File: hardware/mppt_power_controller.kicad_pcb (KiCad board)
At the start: 2 copper layers, 100 x 50 mm, 61 parts, among them J2 USB_B_Micro, J3 Conn_ARM_JTAG_SWD_10, J5 Curiosity Board, Q1 Q_NMOS_GSD, Q2 Q_NMOS_GSD, U1 INA233, U2 PX3519, U3 ATSAMD21G18A-AUT, U4 INA233, U5 TPS61090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

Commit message: Flip solar panel connector around so pin 1 is power and pin 2 is ground like every other board with JST connectors.
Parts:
- J1: renamed from Solar In
- J4: renamed from Battery Out
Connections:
- J1 pad 1: GND -> Net-(C2-Pad2)
- J1 pad 2: Net-(C2-Pad2) -> GND
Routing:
- net Net-(C2-Pad2): track 14.5 -> 15.4 mm
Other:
- rule pad_to_mask_clearance: 0.051 -> 0
- board text added: "Battery"
- board text added: "Solar"
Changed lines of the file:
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@@
   (general
     (thickness 1.6)
-    (drawings 61)
-    (tracks 465)
+    (drawings 63)
+    (tracks 467)
     (modules 61)
     (nets 69)
@@
       (dielectric_constraints no)
     )
-    (last_trace_width 0.3)
+    (last_trace_width 0.75)
     (user_trace_width 0.2)
     (user_trace_width 0.25)
@@
     (pad_size 1.524 1.524)
     (pad_drill 0.762)
-    (pad_to_mask_clearance 0.051)
-    (solder_mask_min_width 0.25)
+    (pad_to_mask_clearance 0)
     (aux_axis_origin 0 0)
     (visible_elements 7FFDFFFF)
@@
     (descr "JST PH series connector, S2B-PH-K (http://www.jst-mfg.com/product/pdf/eng/ePH.pdf), generated with kicad-footprint-generator")
     (tags "connector JST PH top entry")
-    (fp_text reference "Battery Out" (at -2.7 2.35 180) (layer "F.SilkS")
+    (fp_text reference "J4" (at -2.7 2.35 180) (layer "F.SilkS") hide
       (effects (font (size 0.75 0.75) (thickness 0.15)))
     )
@@
     (descr "JST PH series connector, S2B-PH-K (http://www.jst-mfg.com/product/pdf/eng/ePH.pdf), generated with kicad-footprint-generator")
     (tags "connector JST PH top entry")
-    (fp_text reference "Solar In" (at 4.95 2.35 180) (layer "F.SilkS")
+    (fp_text reference "J1" (at 4.95 2.35 180) (layer "F.SilkS") hide
       (effects (font (size 1 1) (thickness 0.15)))
     )
@@
     )
     (pad "2" thru_hole oval (at 2 0 270) (size 1.2 1.75) (drill 0.75) (layers *.Cu *.Mask)
-      (net 3 "Net-(C2-Pad2)"))
-    (pad "1" thru_hole roundrect (at 0 0 270) (size 1.2 1.75) (drill 0.75) (layers *.Cu *.Mask) (roundrect_rratio 0.208333)
       (net 1 "GND"))
+    (pad "1" thru_hole roundrect (at 0 0 270) (size 1.2 1.75) (drill 0.75) (layers *.Cu *.Mask) (roundrect_rratio 0.208333)
+      (net 3 "Net-(C2-Pad2)"))
     (model "${KISYS3DMOD}/Connector_JST.3dshapes/JST_PH_S2B-PH-K_1x02_P2.00mm_Horizontal.wrl"
       (at (xyz 0 0 0))
@@
     )
   )
+  (gr_text "Battery" (at 166.8 77.25) (layer "F.SilkS")
+    (effects (font (size 1 1) (thickness 0.15)))
+  )
+  (gr_text "Solar" (at 74.55 77.4) (layer "F.SilkS")
+    (effects (font (size 1 1) (thickness 0.15)))
+  )
   (gr_text "FET\nPWM" (at 104.65 84.95) (layer "F.SilkS")
     (effects (font (size 1.5 1.5) (thickness 0.15)))
@@
   (gr_line (start 70 110) (end 170 110) (layer "Edge.Cuts") (width 0.05))
   (gr_line (start 70 60) (end 70 110) (layer "Edge.Cuts") (width 0.05))
+  (segment (start 77.6 72) (end 79.4875 73.8875) (width 0.75) (layer "F.Cu") (net 3))
+  (segment (start 79.4875 73.8875) (end 81.6125 73.8875) (width 0.75) (layer "F.Cu") (net 3))
+  (segment (start 76.45 72) (end 77.6 72) (width 0.75) (layer "F.Cu") (net 3))
   (segment (start 155.771766 78) (end 156.5 77.271766) (width 0.3) (layer "F.Cu") (net 1))
   (segment (start 155.025002 77.274998) (end 155.825002 77.274998) (width 0.25) (layer "F.Cu") (net 34))
@@
   (segment (start 85.9625 75.9125) (end 87.8875 75.9125) (width 0.3) (layer "F.Cu") (net 2))
   (segment (start 81.5 74) (end 81.6125 73.8875) (width 0.75) (layer "F.Cu") (net 3))
-  (segment (start 76.45 74) (end 81.5 74) (width 0.75) (layer "F.Cu") (net 3))
   (segment (start 97.85 77.5) (end 97.85 76.325001) (width 0.5) (layer "F.Cu") (net 4))
   (segment (start 98.375 78.5) (end 98.375 78.025) (width 0.5) (layer "F.Cu") (net 4))

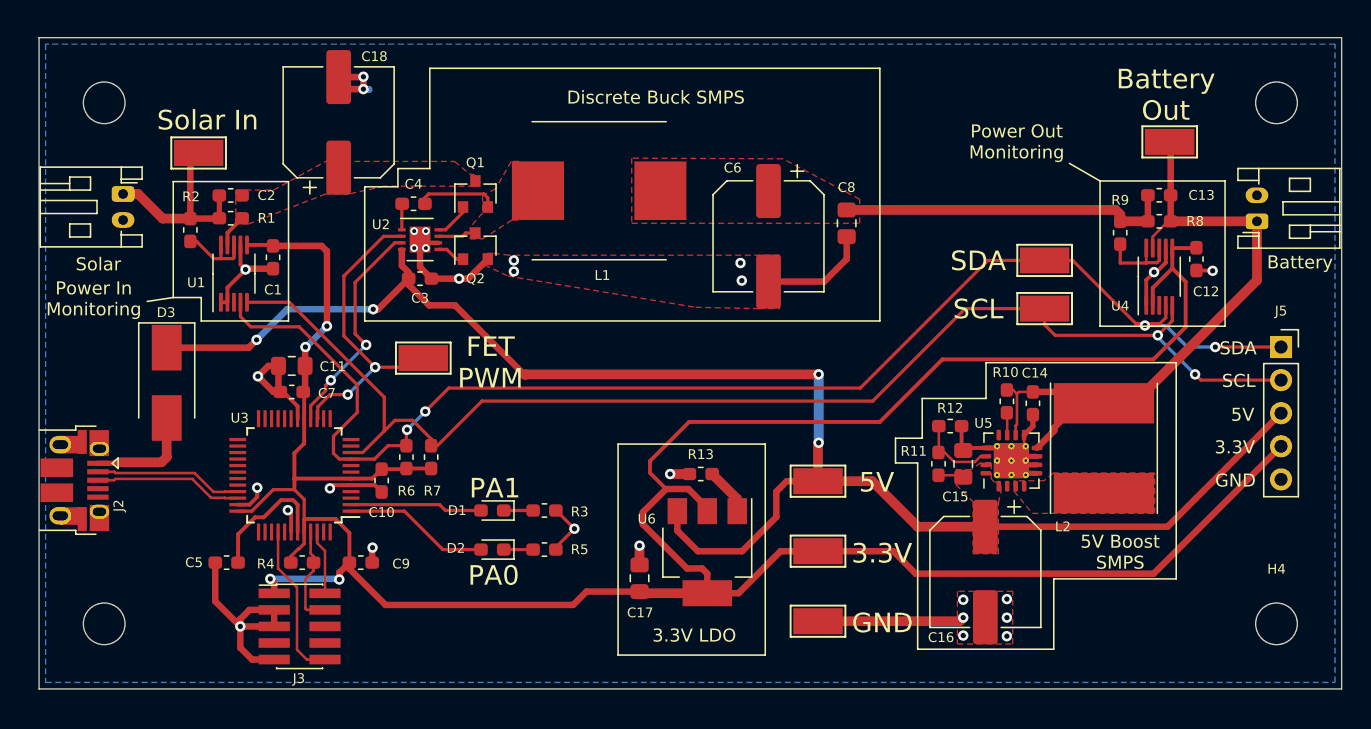
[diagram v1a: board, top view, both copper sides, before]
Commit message: Add some new datasheets, modify code to only flash LEDs as a starting point.
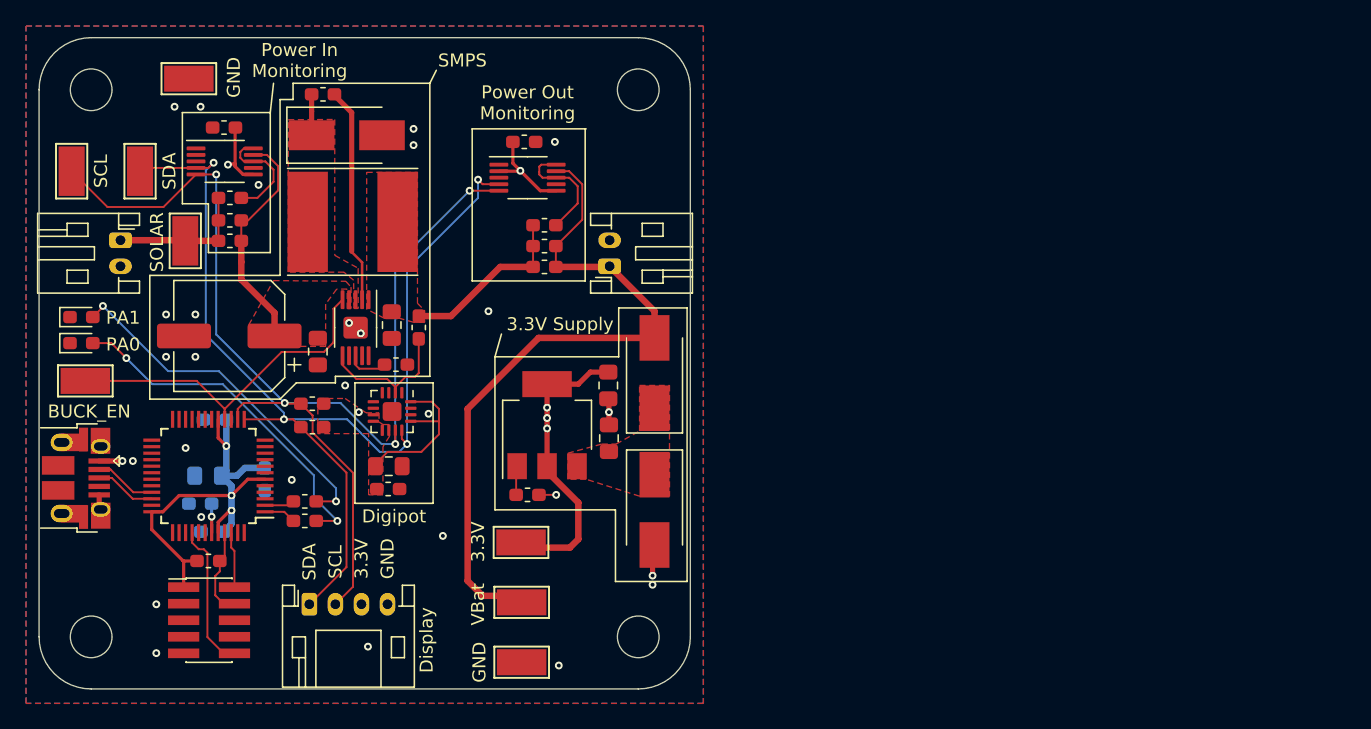
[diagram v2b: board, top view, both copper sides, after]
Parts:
- removed C16, C6: 270uF,16V, Capacitor_SMD:CP_Elec_8x6.9
- removed L2: 10uH, Inductor_SMD:L_Taiyo-Yuden_NR-80xx_HandSoldering
- removed Q1, Q2: Q_NMOS_GSD, Package_TO_SOT_SMD:SOT-23
- removed R12: 200k, Resistor_SMD:R_0603_1608Metric_Pad1.05x0.95mm_HandSolder
- added C19: 0.1uF, Capacitor_SMD:C_0603_1608Metric_Pad1.05x0.95mm_HandSolder, F.Cu at (96.8, 94.7)
- added D4: , Diode_SMD:D_SMB_Handsoldering, F.Cu at (93.6, 67.5)
- added D5: ORing Diode, Diode_SMD:D_SMB_Handsoldering, F.Cu at (117.2, 85.8)
- C10, C11, C5, C7, C9: moved to B.Cu
- C14: value 0.1uF -> 10uF; footprint Capacitor_SMD:C_0603_1608Metric_Pad1.05x0.95mm_HandSolder -> Capacitor_SMD:C_0805_2012Metric_Pad1.15x1.40mm_HandSolder
- C3: value 0.1uF -> 10uF,16V; footprint Capacitor_SMD:C_0603_1608Metric_Pad1.05x0.95mm_HandSolder -> Capacitor_SMD:C_0805_2012Metric_Pad1.15x1.40mm_HandSolder
- C4: value 1nF -> 0.47uF
- J5: value Curiosity Board -> DISPLAY; footprint Connector_PinSocket_2.54mm:PinSocket_1x05_P2.54mm_Vertical -> Connector_JST:JST_PH_S4B-PH-K_1x04_P2.00mm_Horizontal
- L1: value 47uH -> 10UF; footprint Inductor_SMD:L_Taiyo-Yuden_NR-10050_9.8x10.0mm_HandSoldering -> Inductor_SMD:L_Taiyo-Yuden_NR-80xx_HandSoldering
- R10: value 200k -> 120k
- R11: value 1.87M -> 120k
- TP2: value PWM -> GND
- TP5: value 5V -> Buck_EN
- U2: value PX3519 -> LT3971; footprint Package_SON:WSON-8-1EP_3x3mm_P0.5mm_EP1.6x2.0mm -> Package_SO:MSOP-10-1EP_3x3mm_P0.5mm_EP1.68x1.88mm
- U5: value TPS61090 -> AD5141; footprint Package_DFN_QFN:Texas_S-PVQFN-N16_EP2.7x2.7mm_ThermalVias -> Package_DFN_QFN:QFN-16-1EP_3x3mm_P0.5mm_EP1.45x1.45mm
- moved H4 91.0 mm to (74.0, 106.0)
- moved J5 77.2 mm to (90.8, 103.5)
- moved TP4 75.4 mm to (72.5, 70.2), turned to 90 degrees
- moved TP3 69.8 mm to (77.8, 70.2), turned to 90 degrees
- moved TP8 61.0 mm to (107.0, 103.3)
- moved H1 58.0 mm to (116.0, 106.0)
- moved TP5 56.8 mm to (73.5, 86.3), turned to 180 degrees
- moved C12 52.4 mm to (107.2, 68.0), turned to 0 degrees
- moved J4 49.8 mm to (113.8, 77.5)
- moved C14 49.7 mm to (96.8, 92.9), turned to 0 degrees
- moved U4 49.1 mm to (107.5, 70.8), turned to 0 degrees
- moved H2 49.0 mm to (116.0, 64.0)
- moved U5 47.7 mm to (97.1, 88.7), turned to -90 degrees
- moved C13 47.4 mm to (108.8, 76.0)
- moved R8 47.3 mm to (108.8, 77.6)
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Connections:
- C14 pad 1: /VBat -> /3.3V
- C15 pad 1: /5V -> Net-(C15-Pad1)
- C3 pad 1: /5V -> Net-(C18-Pad1)
- D1 pad 1: Net-(D1-Pad1) -> GND
- D2 pad 1: Net-(D2-Pad1) -> GND
- D3 pad 1: /5V -> Net-(C15-Pad1)
- J5 pad 3: /5V -> /3.3V
- J5 pad 4: /3.3V -> GND
- L1 pad 1: Net-(C4-Pad1) -> Net-(C4-Pad2)
- R10 pad 1: /VBat -> Net-(R10-Pad1)
- R10 pad 2: Net-(R10-Pad2) -> GND
- R11 pad 1: /5V -> Net-(C13-Pad2)
- R3 pad 1: GND -> Net-(D1-Pad2)
- R3 pad 2: Net-(D1-Pad1) -> Net-(R3-Pad2)
- R5 pad 1: GND -> Net-(D2-Pad2)
- R5 pad 2: Net-(D2-Pad1) -> Net-(R5-Pad2)
- TP2 pad 1: /FET_PWM -> GND
- TP5 pad 1: /5V -> /Buck_EN
- U2 pad 1: Net-(C4-Pad2) -> Net-(C13-Pad2)
- U2 pad 2: /FET_PWM -> Net-(C4-Pad1)
- U2 pad 3: /FET_ENABLE -> Net-(C4-Pad2)
- U2 pad 4: /5V -> Net-(C18-Pad1)
- U2 pad 5: Net-(Q2-Pad1) -> /Buck_EN
- U2 pad 6: GND -> Net-(R11-Pad2)
- U2 pad 7: Net-(C4-Pad1) -> Net-(U2-Pad7)
- U2 pad 8: Net-(Q1-Pad1) -> Net-(R10-Pad1)
- U2 pad 9: GND -> Net-(U2-Pad9)
- U3 pad 1: Net-(D2-Pad2) -> Net-(R5-Pad2)
- U3 pad 10: /SCL -> Net-(U3-Pad10)
- U3 pad 13: Net-(U3-Pad13) -> /SDA
- U3 pad 14: Net-(U3-Pad14) -> /SCL
- U3 pad 15: /FET_PWM -> Net-(U3-Pad15)
- U3 pad 16: /FET_ENABLE -> /Buck_EN
- U3 pad 2: Net-(D1-Pad2) -> Net-(R3-Pad2)
- U3 pad 9: /SDA -> Net-(U3-Pad9)
- U5 pad 1: /5V -> GND
- U5 pad 10: /VBat -> /3.3V
- U5 pad 11: Net-(R10-Pad2) -> /SCL
- U5 pad 12: Net-(U5-Pad12) -> /SDA
- U5 pad 13: GND -> /3.3V
- U5 pad 14: Net-(R11-Pad2) -> GND
- U5 pad 15: /5V -> GND
- U5 pad 16: /5V -> /3.3V
- U5 pad 2: Net-(U5-Pad2) -> Net-(R11-Pad2)
- U5 pad 3: Net-(L2-Pad2) -> GND
- U5 pad 4: Net-(L2-Pad2) -> GND
- U5 pad 7: GND -> /3.3V
- U5 pad 8: /VBat -> /3.3V
- U5 pad 9: GND -> /3.3V
- U6 pad 3: /5V -> Net-(C15-Pad1)
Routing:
- net /3.3V: track 217.4 -> 82.9 mm, vias 4 -> 9
- net /5V: track 125.8 -> 0.00 mm, vias 4 -> 0
- net GND: track 107.2 -> 5.00 mm, vias 29 -> 22
- net /Vusb: track 8.48 -> 63.2 mm, vias 0 -> 4
- net /Buck_EN: track 0.00 -> 26.4 mm
- net /FET_PWM: track 24.3 -> 0.00 mm, vias 2 -> 0
- net /SDA: track 103.6 -> 85.4 mm
- net /FET_ENABLE: track 17.4 -> 0.00 mm, vias 2 -> 0
- net Net-(D1-Pad2): track 10.2 -> 27.4 mm, vias 0 -> 2
- net Net-(D2-Pad2): track 11.2 -> 27.0 mm, vias 0 -> 2
- net Net-(C18-Pad1): track 2.52 -> 17.8 mm
- net Net-(C13-Pad2): track 25.8 -> 14.0 mm
- net /SCL: track 99.9 -> 91.4 mm, vias 2 -> 4
- net Net-(C5-Pad2): track 10.1 -> 2.22 mm, vias 0 -> 1
- net Net-(C4-Pad1): track 9.19 -> 16.6 mm
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- added copper zone on 3V3.Cu, net /3.3V
- added copper zone on F.Cu, net /3.3V
- added copper zone on GND.Cu, net GND
- added copper zone on F.Cu, net Net-(C15-Pad1)
- added copper zone on F.Cu, net Net-(C4-Pad2)
- removed copper zone on F.Cu, net /5V
- removed copper zone on F.Cu, net Net-(C4-Pad1)
- removed copper zone on F.Cu, net Net-(L2-Pad2)
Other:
- board size 100 x 50 mm -> 50 x 50 mm
- copper layers 2 -> 4
- rule trace_min: 0.13 -> 0.0889
- rule via_min_drill: 0.3 -> 0.2
- rule via_min_size: 0.4 -> 0.45
- board text added: "3.3V Supply"
- board text added: "BUCK_EN"
- board text added: "Digipot"
- board text added: "Display"
- board text added: "SMPS"
- board text added: "SOLAR"
- board text added: "Solar MPPT Jon Neal, March 2020 EECE 5138C"
- board text added: "VBat"
- board text removed: "3.3V LDO"
- board text removed: "5V"
- board text removed: "5V Boost SMPS"
- board text removed: "Battery"
- board text removed: "Battery Out"
- board text removed: "Discrete Buck SMPS"
- board text removed: "FET PWM"
- board text removed: "Solar"
- board text removed: "Solar In"
- board text removed: "Solar MPPT Buck Power Supply Jon Neal, Nov 2019 EECE 4038C"
